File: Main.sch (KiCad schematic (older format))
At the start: 39 parts, among them J1 Conn_01x01_Female, J2 Conn_01x01_Female, J3 Conn_01x01_Female, J4 Conn_01x02_Female, J5 Conn_01x01_Female, Q1 CSD17307Q5A, Q2 CSD17307Q5A, Q3 Si6435ADQ, SW1 SW_Push, SW2 SW_Push, SW3 SW_Push, U1 LTC4002ES8-4.2, U2 BQ297xy, U3 LTC6995-1, U4 TPS2557

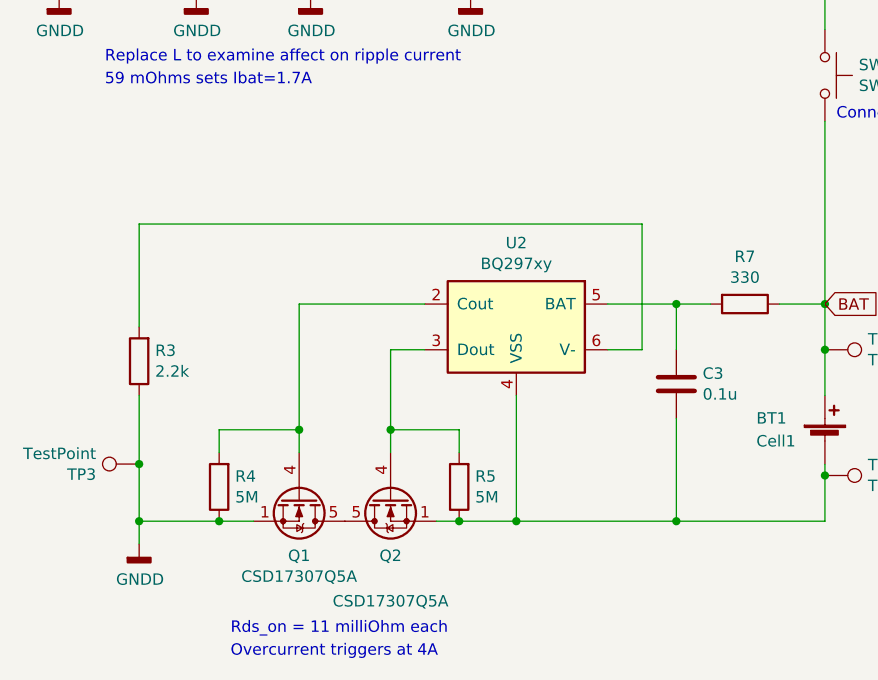
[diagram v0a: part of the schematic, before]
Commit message: still need breakout board for bq29707
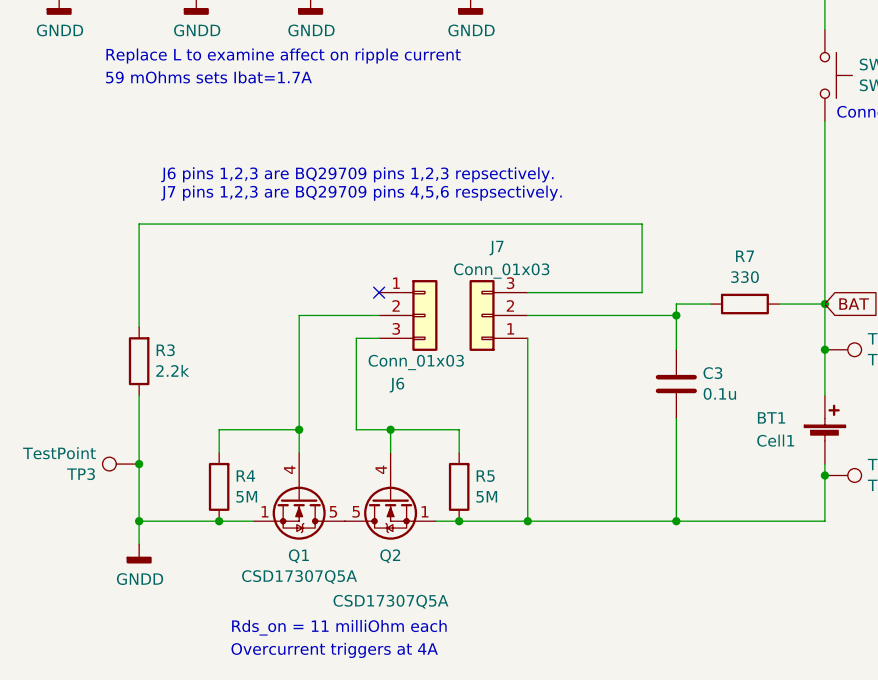
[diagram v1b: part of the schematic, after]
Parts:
- removed U2: BQ297xy, Package_SON:WSON-6_1.5x1.5mm_P0.5mm, symbol Battery_Management:BQ297xy
- added J6, J7: Conn_01x03, Connector_PinSocket_2.00mm:PinSocket_1x03_P2.00mm_Vertical, symbol Connector_Generic:Conn_01x03
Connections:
- net at BT1.2 (-), C3.2, Q2.1 (S)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: now also J7.1 (Pin_1)
- net at Q1.4 (G), R4.2: now also J6.2 (Pin_2)
- net at Q2.4 (G), R5.2: now also J6.3 (Pin_3)
- net at C3.1, R7.2: now also J7.2 (Pin_2)
- net at R3.2: now also J7.3 (Pin_3)
- no-connect marks 3 -> 4
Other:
- note added: "J6 pins 1,2,3 are BQ29709 pins 1,2,3 repsectively.\nJ7 pins 1,2,3 are BQ29709 pins 4,5,6 respsectively."
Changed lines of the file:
@@
 $EndComp
-$Comp
-L Battery_Management:BQ297xy U2
-U 1 1 5D06CFBB
-P 5550 7750
-AR Path="/5D06CFBB" Ref="U2"  Part="1"
-AR Path="/5D07F3FC/5D06CFBB" Ref="U?"  Part="1"
-AR Path="/5D0A75A0/5D06CFBB" Ref="U?"  Part="1"
-AR Path="/5D0B1FBC/5D06CFBB" Ref="U?"  Part="1"
-AR Path="/5D0BC9BA/5D06CFBB" Ref="U?"  Part="1"
-F 0 "U2" H 5550 8117 50  0000 C CNN
-F 1 "BQ297xy" H 5550 8026 50  0000 C CNN
-F 2 "Package_SON:WSON-6_1.5x1.5mm_P0.5mm" H 5550 8100 50  0001 C CNN
-F 3 "http://www.ti.com/lit/ds/symlink/bq2970.pdf" H 5300 7950 50  0001 C CNN
-	1    5550 7750
-	-1   0    0    -1
-$EndComp
-Wire Wire Line
-	5150 7850 5000 7850
-Wire Wire Line
-	5150 7650 4600 7650
-Wire Wire Line
-	5550 8600 5300 8600
 $Comp
 L Device:R R7
@@
 $EndComp
 Wire Wire Line
-	5950 7650 6250 7650
-Wire Wire Line
 	6700 7650 6900 7650
 $Comp
@@
 $EndComp
 Wire Wire Line
-	6250 7850 6250 7650
-Connection ~ 6250 7650
+	6250 7850 6250 7700
 Wire Wire Line
 	6250 7650 6400 7650
-Wire Wire Line
-	5550 8600 6250 8600
-Connection ~ 5550 8600
 Connection ~ 6250 8600
 Wire Wire Line
 	6250 8600 6900 8600
-Wire Wire Line
-	5950 7850 6100 7850
-Wire Wire Line
-	6100 7850 6100 7300
 Wire Wire Line
 	3900 7300 3900 7750
@@
 	6250 8150 6250 8600
 Wire Wire Line
-	5550 8050 5550 8600
-Wire Wire Line
-	5000 7850 5000 8200
-Wire Wire Line
-	4600 7650 4600 8200
-Wire Wire Line
 	3900 8050 3900 8350
 $Comp
@@
 	-1   0    0    1
 $EndComp
-Wire Wire Line
-	3900 7300 6100 7300
 Connection ~ 4250 8600
 Wire Wire Line
@@
 Wire Wire Line
 	4250 8200 4600 8200
-Connection ~ 4600 8200
 Wire Wire Line
 	4600 8200 4600 8300
@@
 Wire Wire Line
 	5300 8200 5000 8200
-Connection ~ 5000 8200
 Wire Wire Line
 	5000 8200 5000 8300
@@
 	1    0    0    -1
 $EndComp
+$Comp
+L Connector_Generic:Conn_01x03 J6
+U 1 1 5D115F12
+P 5150 7700
+F 0 "J6" H 5000 7400 50  0000 L CNN
+F 1 "Conn_01x03" H 4900 7500 50  0000 L CNN
+F 2 "Connector_PinSocket_2.00mm:PinSocket_1x03_P2.00mm_Vertical" H 5150 7700 50  0001 C CNN
+F 3 "~" H 5150 7700 50  0001 C CNN
+	1    5150 7700
+	1    0    0    -1
+$EndComp
+Wire Wire Line
+	3900 7300 6100 7300
+Wire Wire Line
+	5000 8200 4850 8200
+Wire Wire Line
+	4850 8200 4850 7800
+Wire Wire Line
+	4850 7800 4950 7800
+Connection ~ 5000 8200
+Wire Wire Line
+	4600 8200 4600 7700
+Wire Wire Line
+	4600 7700 4950 7700
+Connection ~ 4600 8200
+Wire Wire Line
+	6100 7600 5600 7600
+Wire Wire Line
+	6100 7300 6100 7600
+Wire Wire Line
+	5600 7700 6250 7700
+Connection ~ 6250 7700
+Wire Wire Line
+	6250 7700 6250 7650
+Wire Wire Line
+	5300 8600 5600 8600
+$Comp
+L Connector_Generic:Conn_01x03 J7
+U 1 1 5D147C15
+P 5400 7700
+F 0 "J7" H 5300 7400 50  0000 L CNN
+F 1 "Conn_01x03" H 5100 7500 50  0000 L CNN
+F 2 "Connector_PinSocket_2.00mm:PinSocket_1x03_P2.00mm_Vertical" H 5400 7700 50  0001 C CNN
+F 3 "~" H 5400 7700 50  0001 C CNN
+	1    5400 7700
+	-1   0    0    1
+$EndComp
+Wire Wire Line
+	5600 7800 5600 8600
+Connection ~ 5600 8600
+Wire Wire Line
+	5600 8600 6250 8600
+NoConn ~ 4950 7600
+Text Notes 4000 7200 0    50   ~ 0
+J6 pins 1,2,3 are BQ29709 pins 1,2,3 repsectively.\nJ7 pins 1,2,3 are BQ29709 pins 4,5,6 respsectively.
 $EndSCHEMATC

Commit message: Finished, should be reviewed
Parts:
- added TP4: TestPoint, Connector_PinHeader_2.00mm:PinHeader_1x01_P2.00mm_Vertical, symbol Connector:TestPoint
- J6, J7: footprint Connector_PinSocket_2.00mm:PinSocket_1x03_P2.00mm_Vertical -> Connector_PinSocket_2.54mm:PinSocket_1x03_P2.54mm_Vertical
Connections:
- net at C7.1, R12.1, U4.7 (OUT): now also TP4.1
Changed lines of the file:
@@
 F 0 "J6" H 5000 7400 50  0000 L CNN
 F 1 "Conn_01x03" H 4900 7500 50  0000 L CNN
-F 2 "Connector_PinSocket_2.00mm:PinSocket_1x03_P2.00mm_Vertical" H 5150 7700 50  0001 C CNN
+F 2 "Connector_PinSocket_2.54mm:PinSocket_1x03_P2.54mm_Vertical" H 5150 7700 50  0001 C CNN
 F 3 "~" H 5150 7700 50  0001 C CNN
 	1    5150 7700
@@
 F 0 "J7" H 5300 7400 50  0000 L CNN
 F 1 "Conn_01x03" H 5100 7500 50  0000 L CNN
-F 2 "Connector_PinSocket_2.00mm:PinSocket_1x03_P2.00mm_Vertical" H 5400 7700 50  0001 C CNN
+F 2 "Connector_PinSocket_2.54mm:PinSocket_1x03_P2.54mm_Vertical" H 5400 7700 50  0001 C CNN
 F 3 "~" H 5400 7700 50  0001 C CNN
 	1    5400 7700
@@
 Text Notes 4000 7200 0    50   ~ 0
 J6 pins 1,2,3 are BQ29709 pins 1,2,3 repsectively.\nJ7 pins 1,2,3 are BQ29709 pins 4,5,6 respsectively.
+$Comp
+L Connector:TestPoint TP4
+U 1 1 5D14B430
+P 13750 4350
+F 0 "TP4" V 13704 4538 50  0000 L CNN
+F 1 "TestPoint" V 13795 4538 50  0000 L CNN
+F 2 "Connector_PinHeader_2.00mm:PinHeader_1x01_P2.00mm_Vertical" H 13950 4350 50  0001 C CNN
+F 3 "~" H 13950 4350 50  0001 C CNN
+	1    13750 4350
+	0    1    1    0
+$EndComp
+Wire Wire Line
+	13300 4350 13750 4350
+Connection ~ 13300 4350
 $EndSCHEMATC

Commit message: reviewed footprints
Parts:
- U3: footprint Package_TO_SOT_SMD:TSOT-23-6 -> Package_TO_SOT_SMD:TSOT-23-6_HandSoldering
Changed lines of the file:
@@
 F 0 "U3" H 9525 6165 50  0000 C CNN
 F 1 "LTC6995-1" H 9525 6074 50  0000 C CNN
-F 2 "Package_TO_SOT_SMD:TSOT-23-6" H 9550 5650 50  0001 C CNN
+F 2 "Package_TO_SOT_SMD:TSOT-23-6_HandSoldering" H 9550 5650 50  0001 C CNN
 F 3 "" H 9550 5650 50  0001 C CNN
 	1    9550 5650

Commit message: added changes mark wante
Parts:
- removed D3: LED, LED_SMD:LED_1206_3216Metric, symbol Device:LED
- removed L1: 1.64u, Inductor_SMD:L_1206_3216Metric, symbol Device:L
- removed R11: 20k, Resistor_SMD:R_1206_3216Metric, symbol Device:R
- removed R12: 2k, Resistor_SMD:R_1206_3216Metric, symbol Device:R
- added J10, J11, J12, J9: Conn_01x01_Female, Connector_PinSocket_2.00mm:PinSocket_1x01_P2.00mm_Vertical, symbol Connector:Conn_01x01_Female
- added J8: Conn_01x06, Connector_PinHeader_2.00mm:PinHeader_1x06_P2.00mm_Vertical, symbol Connector_Generic:Conn_01x06
- added SW4: SW_Push, Button_Switch_SMD:SW_DIP_SPSTx01_Slide_6.7x4.1mm_W6.73mm_P2.54mm_LowProfile_JPin, symbol Switch:SW_Push
- added TP5, TP6: TestPoint, Connector_PinHeader_2.00mm:PinHeader_1x01_P2.00mm_Vertical, symbol Connector:TestPoint
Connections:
- net GNDD: now also J10.1 (Pin_1)
- net BQ29707_P4: now reaches BT1.2 (-), C3.2, J7.1 (Pin_1), Q2.1 (S), Q2.2 (S), Q2.3 (S), R5.1, TP2.1
- net BQ29707_P4: now also J8.4 (Pin_4)
- net BQ29707_P5: now reaches C3.1, J7.2 (Pin_2), R7.2
- net BQ29707_P5: now also J8.5 (Pin_5)
- net BQ29707_P6: now reaches J7.3 (Pin_3), R3.2
- net BQ29707_P6: now also J8.6 (Pin_6)
- net BQ29707_P3: now reaches J6.3 (Pin_3), Q2.4 (G), R5.2
- net BQ29707_P3: now also J8.3 (Pin_3)
- net BQ29707_P2: now reaches J6.2 (Pin_2), Q1.4 (G), R4.2
- net BQ29707_P2: now also J8.2 (Pin_2)
- net at U1.1 (COMP): now also SW4.2; no longer C1.1
- net at C2.1, R6.2, SW1.1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: now also TP5.1
- net at R6.1, U1.7 (SENSE): now also J12.1 (Pin_1), TP6.1
- net at D2.1 (K), Q3.2 (D): now also J11.1 (Pin_1)
- net at U4.5 (ILIM): now also J9.1 (Pin_1)
- net BQ29707_P1: now reaches J6.1 (Pin_1)
- net BQ29707_P1: now also J8.1 (Pin_1)
- new net: C1.1, SW4.1
- no-connect marks 4 -> 3
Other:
- note added: "20k"
- moved on the sheet: C1, C7, D2, R2

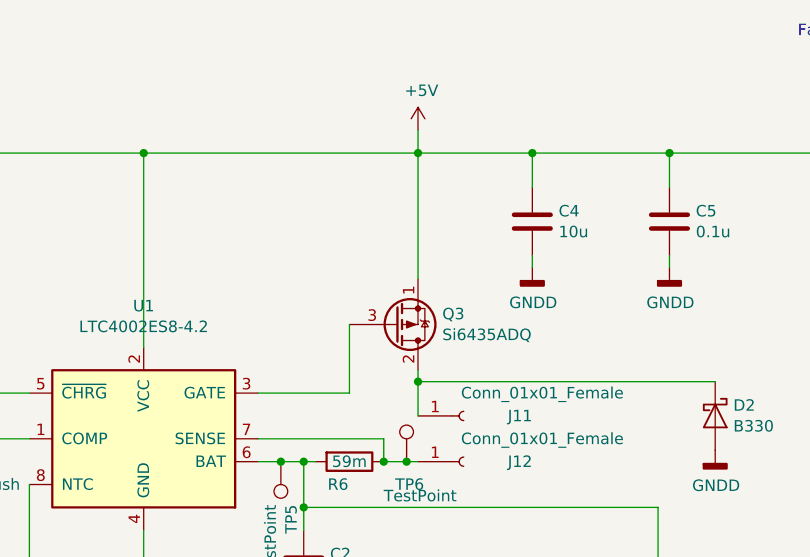
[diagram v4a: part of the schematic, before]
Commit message: changed transistor
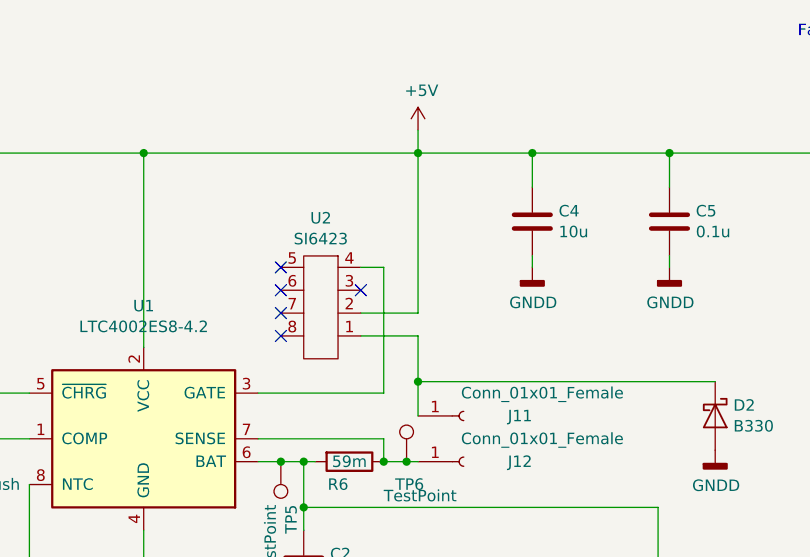
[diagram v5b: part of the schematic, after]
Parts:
- removed Q3: Si6435ADQ, Package_SO:TSSOP-8_4.4x3mm_P0.65mm, symbol Device:Q_PMOS_SDG
- added U2: SI6423, Package_SO:TSSOP-8_4.4x3mm_P0.65mm, symbol SI6423:SI6423
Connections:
- net +5V: now also U2.2
- net at U1.3 (GATE): now also U2.4
- net at D2.1 (K), J11.1 (Pin_1): now also U2.1
- no-connect marks 3 -> 8
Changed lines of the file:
@@
 	1    0    0    -1
 $EndComp
-$Comp
-L Device:Q_PMOS_SDG Q3
-U 1 1 5D084F7F
-P 5750 5100
-F 0 "Q3" H 5956 5054 50  0000 L CNN
-F 1 "Si6435ADQ" H 5956 5145 50  0000 L CNN
-F 2 "Package_SO:TSSOP-8_4.4x3mm_P0.65mm" H 5950 5200 50  0001 C CNN
-F 3 "~" H 5750 5100 50  0001 C CNN
-	1    5750 5100
-	1    0    0    1
-$EndComp
-Wire Wire Line
-	5150 5400 5550 5400
-Wire Wire Line
-	5850 5300 5850 5350
 Connection ~ 5850 5350
-Wire Wire Line
-	5550 5100 5550 5400
 $Comp
 L Device:C C1
@@
 Wire Wire Line
 	6350 4350 6950 4350
-Wire Wire Line
-	5850 4900 5850 4350
 Connection ~ 5850 4350
 Wire Wire Line
@@
 Wire Wire Line
 	3300 5600 3300 5650
+$Comp
+L SI6423:SI6423 U2
+U 1 1 5D1BA352
+P 5350 5000
+F 0 "U2" H 5275 4635 50  0000 C CNN
+F 1 "SI6423" H 5275 4726 50  0000 C CNN
+F 2 "Package_SO:TSSOP-8_4.4x3mm_P0.65mm" H 5000 5250 50  0001 C CNN
+F 3 "" H 5000 5250 50  0001 C CNN
+	1    5350 5000
+	-1   0    0    1
+$EndComp
+Wire Wire Line
+	5850 5050 5600 5050
+Wire Wire Line
+	5850 4350 5850 5050
+Wire Wire Line
+	5850 5150 5600 5150
+Wire Wire Line
+	5850 5150 5850 5350
+Wire Wire Line
+	5700 5400 5700 4850
+Wire Wire Line
+	5700 4850 5600 4850
+Wire Wire Line
+	5150 5400 5700 5400
+NoConn ~ 5250 4850
+NoConn ~ 5250 4950
+NoConn ~ 5250 5050
+NoConn ~ 5250 5150
+NoConn ~ 5600 4950
 $EndSCHEMATC
